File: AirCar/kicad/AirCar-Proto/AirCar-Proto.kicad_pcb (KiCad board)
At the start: 2 copper layers, 1 part, among them U1 Pico

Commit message: work on proto
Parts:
- added D1: D_Schottky, Diode_THT:D_DO-41_SOD81_P7.62mm_Horizontal, F.Cu at (167.6, 39.4)
- added H1: MountingHole, MountingHole:MountingHole_3.2mm_M3, F.Cu at (68.6, 37.1)
- added H2: MountingHole, MountingHole:MountingHole_3.2mm_M3, F.Cu at (68.6, 45.1)
- added H3: MountingHole, MountingHole:MountingHole_3.2mm_M3, F.Cu at (68.6, 53.0)
- added H4: MountingHole, MountingHole:MountingHole_3.2mm_M3, F.Cu at (68.6, 61.0)
- added J1: Conn_01x05, Connector_PinHeader_2.54mm:PinHeader_1x05_P2.54mm_Horizontal, F.Cu at (104.1, 68.6)
- added J2: Barrel_Jack, Connector_BarrelJack:BarrelJack_CUI_PJ-102AH_Horizontal, F.Cu at (157.5, 39.0)
- added J3: Conn_01x06, Connector_PinHeader_2.54mm:PinHeader_1x06_P2.54mm_Horizontal, F.Cu at (177.8, 48.3)
- added SW1: SW_Push, Library:SW4_1825910-B_TEC, F.Cu at (173.4, 75.9)
- added SW2: SW_SPDT, Library:CS12ANW03_NKK, F.Cu at (154.9, 48.3)
- added SW3: SW_Push, Library:SW4_1825910-B_TEC, F.Cu at (160.7, 75.9)
- moved U1 40.1 mm to (133.3, 54.6), turned to 180 degrees
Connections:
- U1 pad 18: unconnected-(U1-GND-Pad18) -> GND
- U1 pad 23: Net-(J1-Pin_1) -> GND
- U1 pad 28: unconnected-(U1-GND-Pad28) -> GND
- U1 pad 3: unconnected-(U1-GND-Pad3) -> GND
- U1 pad 33: unconnected-(U1-AGND-Pad33) -> GND
- U1 pad 39: Net-(D1-K) -> /VSYS
- U1 pad 42: Net-(J3-Pin_2) -> GND
- U1 pad 8: unconnected-(U1-GND-Pad8) -> GND
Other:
- board outline added: 83.8 x 55.9 mm

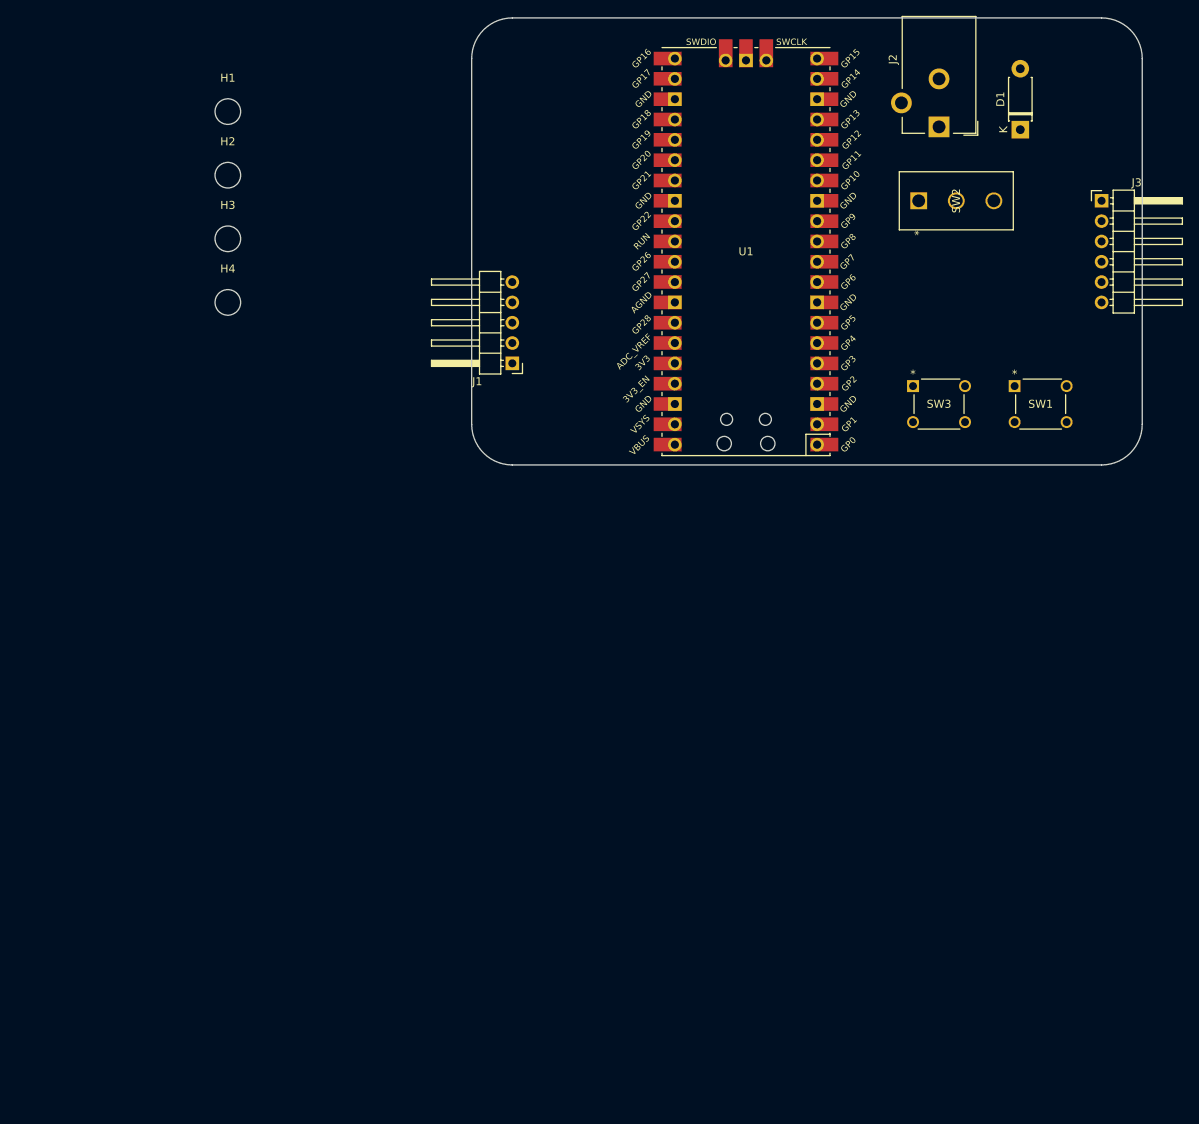
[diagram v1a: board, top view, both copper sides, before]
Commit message: Good start.
Need to add 3v/5v option for encoder.
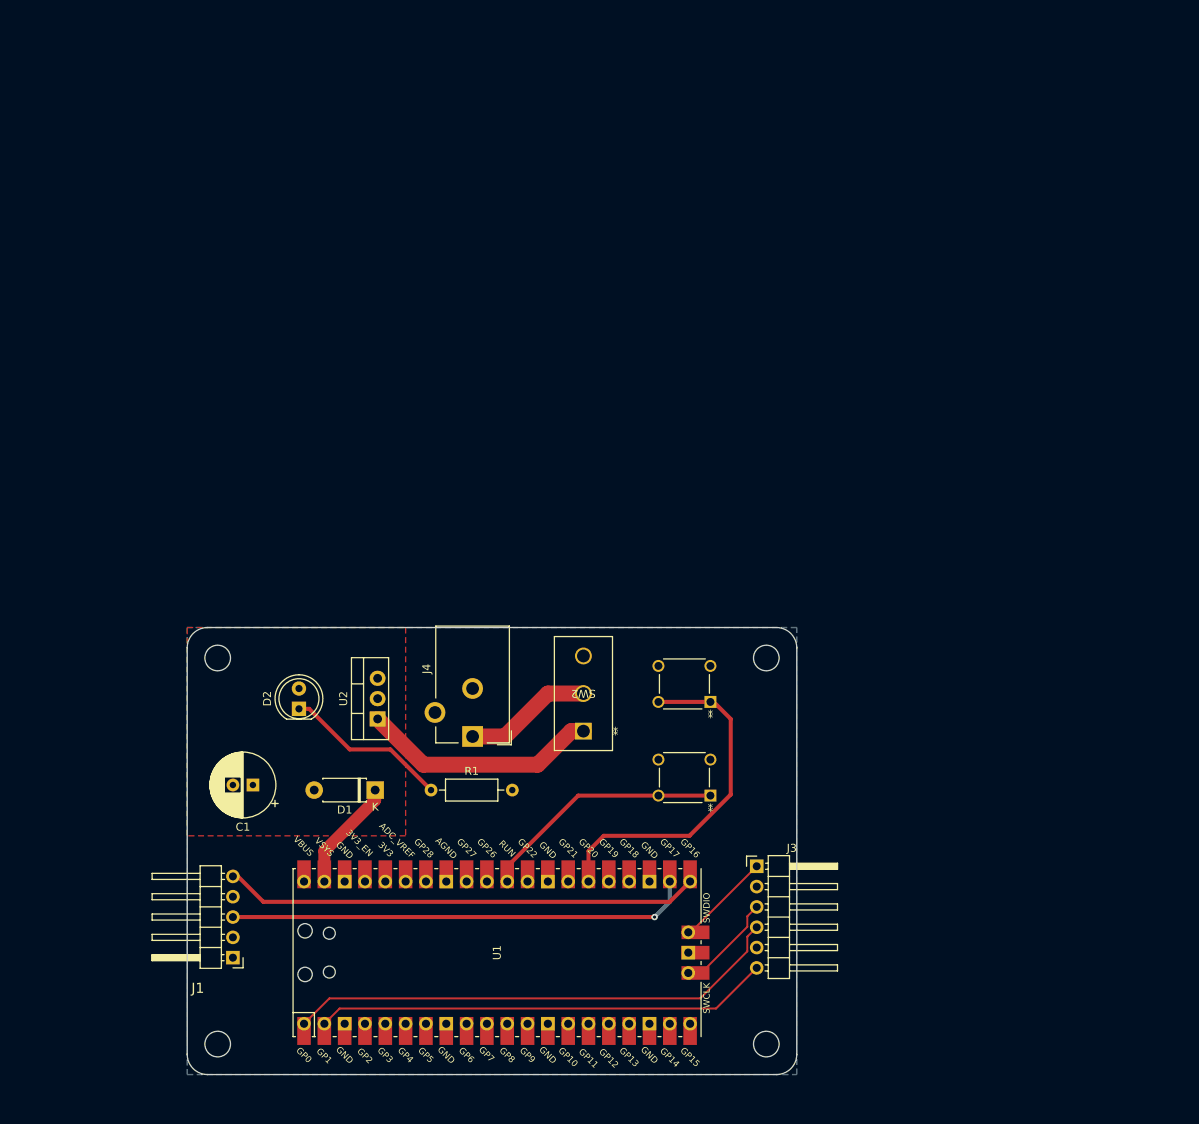
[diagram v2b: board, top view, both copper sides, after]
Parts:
- removed J2: Barrel_Jack, Connector_BarrelJack:BarrelJack_CUI_PJ-102AH_Horizontal
- removed SW1, SW3: SW_Push, Library:SW4_1825910-B_TEC
- added C1: 50uF, Capacitor_THT:CP_Radial_D8.0mm_P2.50mm, F.Cu at (71.7, 121.3)
- added D2: Green, LED_THT:LED_D5.0mm, F.Cu at (77.5, 111.8)
- added J4: PJ-102A, Connector_BarrelJack:BarrelJack_CUI_PJ-102AH_Horizontal, F.Cu at (99.2, 115.2)
- added R1: 1K, Resistor_THT:R_Axial_DIN0207_L6.3mm_D2.5mm_P10.16mm_Horizontal, F.Cu at (94.0, 121.9)
- added Reset1: SmallPushbutton, Library:SW4_1825910-B_TEC, F.Cu at (122.4, 118.1)
- added U2: LM7805_TO220, Package_TO_SOT_THT:TO-220-3_Vertical, F.Cu at (87.3, 113.0)
- added USER1: SmallPushbutton, Library:SW4_1825910-B_TEC, F.Cu at (122.4, 106.4)
- moved H3 121.1 mm to (135.9, 153.7)
- moved D1 115.4 mm to (87.0, 121.9), turned to 180 degrees
- moved J3 93.7 mm to (134.7, 131.4)
- moved U1 93.0 mm to (102.2, 142.2), turned to 90 degrees
- moved H4 92.7 mm to (67.3, 153.7)
- moved H2 90.4 mm to (135.9, 105.4)
- moved J1 82.1 mm to (69.2, 142.9)
- moved SW2 78.4 mm to (113.0, 114.6), turned to 180 degrees
- moved H1 68.3 mm to (67.3, 105.4)
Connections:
- D1 pad 2: Net-(D1-A) -> /V5p0
- SW2 pad 1: unconnected-(SW2-A-Pad1) -> /V9P0_SW
- SW2 pad 2: Net-(SW2-B) -> /V9P0
- SW2 pad 3: Net-(D1-A) -> unconnected-(SW2-C-Pad3)
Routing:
- net /PicoTx: track 0.00 -> 62.7 mm
- net /Lag: track 0.00 -> 59.5 mm
- net /Lead: track 0.00 -> 57.9 mm, vias 0 -> 1
- net /PicoRx: track 0.00 -> 56.9 mm
- net Net-(U1-GPIO20): track 0.00 -> 43.9 mm
- net Net-(U1-RUN): track 0.00 -> 30.9 mm
- net /V9P0_SW: track 0.00 -> 29.8 mm
- net Net-(D2-K): track 0.00 -> 20.7 mm
- net /V9P0: track 0.00 -> 16.1 mm
- net /VSYS: track 0.00 -> 14.1 mm
- net Net-(J3-Pin_3): track 0.00 -> 12.7 mm
- net Net-(J3-Pin_1): track 0.00 -> 12.0 mm
- added copper zone on F.Cu, net /V5p0
- added copper zone on B.Cu, net GND
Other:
- board size 83.8 x 55.9 mm -> 76.2 x 55.9 mm
- board text added: "Mounting Holes are for M3 posts."
